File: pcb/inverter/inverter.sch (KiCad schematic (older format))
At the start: 44 parts, among them J1 Conn_01x01_Female, J2 Conn_01x01_Female, J3 Conn_01x01_Female, J4 Conn_01x01_Female, J5 Conn_01x02_Male, J6 Conn_01x02_Male, J7 Conn_01x02_Male, J8 Conn_01x02_Male, Q1 IRG4PF50W, Q2 IRG4PF50W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

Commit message: inverter PCB layout finished
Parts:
- added J1001, J1002, J1003, J1004: mounting-hole-nc, wbraun_smd:M3-through-hole, symbol wbraun_ic_lib:mounting-hole-nc
- added J1005, J1006, J1007, J1008: mounting-hole-grounded, wbraun_smd:M3-tight-fit-pan-head, symbol wbraun_ic_lib:mounting-hole-grounded
- R1, R10, R11, R12, R13, R14, R15, R16, R2, R3, R4, R5, R6, R7, R8, R9: footprint Resistor_SMD:R_0805_2012Metric -> Resistor_SMD:R_1206_3216Metric
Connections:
- net VIN+: now also J1007.1
- net VIN-: now also J1008.1
- net VSW+: now also J1005.1
- net VSW-: now also J1006.1
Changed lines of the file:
@@
 F 0 "R3" V 2900 3700 50  0000 C CNN
 F 1 "R" V 2700 3700 50  0000 C CNN
-F 2 "Resistor_SMD:R_0805_2012Metric" V 2730 3500 50  0001 C CNN
+F 2 "Resistor_SMD:R_1206_3216Metric" V 2730 3500 50  0001 C CNN
 F 3 "~" H 2800 3500 50  0001 C CNN
 	1    2800 3500
@@
 F 0 "R1" V 2850 2850 50  0000 C CNN
 F 1 "R" V 2700 2900 50  0000 C CNN
-F 2 "Resistor_SMD:R_0805_2012Metric" V 2730 2650 50  0001 C CNN
+F 2 "Resistor_SMD:R_1206_3216Metric" V 2730 2650 50  0001 C CNN
 F 3 "~" H 2800 2650 50  0001 C CNN
 	1    2800 2650
@@
 F 0 "R2" V 2593 3000 50  0000 C CNN
 F 1 "R" V 2684 3000 50  0000 C CNN
-F 2 "Resistor_SMD:R_0805_2012Metric" V 2730 3000 50  0001 C CNN
+F 2 "Resistor_SMD:R_1206_3216Metric" V 2730 3000 50  0001 C CNN
 F 3 "~" H 2800 3000 50  0001 C CNN
 	1    2800 3000
@@
 F 0 "R4" V 2593 3850 50  0000 C CNN
 F 1 "R" V 2684 3850 50  0000 C CNN
-F 2 "Resistor_SMD:R_0805_2012Metric" V 2730 3850 50  0001 C CNN
+F 2 "Resistor_SMD:R_1206_3216Metric" V 2730 3850 50  0001 C CNN
 F 3 "~" H 2800 3850 50  0001 C CNN
 	1    2800 3850
@@
 F 0 "R5" V 4250 2900 50  0000 C CNN
 F 1 "R" V 4400 2800 50  0000 C CNN
-F 2 "Resistor_SMD:R_0805_2012Metric" V 4280 2650 50  0001 C CNN
+F 2 "Resistor_SMD:R_1206_3216Metric" V 4280 2650 50  0001 C CNN
 F 3 "~" H 4350 2650 50  0001 C CNN
 	1    4350 2650
@@
 F 0 "R7" V 4150 3750 50  0000 C CNN
 F 1 "R" V 4250 3700 50  0000 C CNN
-F 2 "Resistor_SMD:R_0805_2012Metric" V 4280 3500 50  0001 C CNN
+F 2 "Resistor_SMD:R_1206_3216Metric" V 4280 3500 50  0001 C CNN
 F 3 "~" H 4350 3500 50  0001 C CNN
 	1    4350 3500
@@
 F 0 "R8" V 4143 3850 50  0000 C CNN
 F 1 "R" V 4234 3850 50  0000 C CNN
-F 2 "Resistor_SMD:R_0805_2012Metric" V 4280 3850 50  0001 C CNN
+F 2 "Resistor_SMD:R_1206_3216Metric" V 4280 3850 50  0001 C CNN
 F 3 "~" H 4350 3850 50  0001 C CNN
 	1    4350 3850
@@
 F 0 "R6" V 4143 3000 50  0000 C CNN
 F 1 "R" V 4234 3000 50  0000 C CNN
-F 2 "Resistor_SMD:R_0805_2012Metric" V 4280 3000 50  0001 C CNN
+F 2 "Resistor_SMD:R_1206_3216Metric" V 4280 3000 50  0001 C CNN
 F 3 "~" H 4350 3000 50  0001 C CNN
 	1    4350 3000
@@
 F 0 "R11" V 6700 3850 50  0000 C CNN
 F 1 "R" V 6900 3750 50  0000 C CNN
-F 2 "Resistor_SMD:R_0805_2012Metric" V 6780 3550 50  0001 C CNN
+F 2 "Resistor_SMD:R_1206_3216Metric" V 6780 3550 50  0001 C CNN
 F 3 "~" H 6850 3550 50  0001 C CNN
 	1    6850 3550
@@
 F 0 "R9" V 7000 2900 50  0000 C CNN
 F 1 "R" V 6900 2900 50  0000 C CNN
-F 2 "Resistor_SMD:R_0805_2012Metric" V 6780 2700 50  0001 C CNN
+F 2 "Resistor_SMD:R_1206_3216Metric" V 6780 2700 50  0001 C CNN
 F 3 "~" H 6850 2700 50  0001 C CNN
 	1    6850 2700
@@
 F 0 "R10" V 6643 3050 50  0000 C CNN
 F 1 "R" V 6734 3050 50  0000 C CNN
-F 2 "Resistor_SMD:R_0805_2012Metric" V 6780 3050 50  0001 C CNN
+F 2 "Resistor_SMD:R_1206_3216Metric" V 6780 3050 50  0001 C CNN
 F 3 "~" H 6850 3050 50  0001 C CNN
 	1    6850 3050
@@
 F 0 "R12" V 6643 3900 50  0000 C CNN
 F 1 "R" V 6734 3900 50  0000 C CNN
-F 2 "Resistor_SMD:R_0805_2012Metric" V 6780 3900 50  0001 C CNN
+F 2 "Resistor_SMD:R_1206_3216Metric" V 6780 3900 50  0001 C CNN
 F 3 "~" H 6850 3900 50  0001 C CNN
 	1    6850 3900
@@
 F 0 "R13" V 8200 2950 50  0000 C CNN
 F 1 "R" V 8300 2900 50  0000 C CNN
-F 2 "Resistor_SMD:R_0805_2012Metric" V 8330 2700 50  0001 C CNN
+F 2 "Resistor_SMD:R_1206_3216Metric" V 8330 2700 50  0001 C CNN
 F 3 "~" H 8400 2700 50  0001 C CNN
 	1    8400 2700
@@
 F 0 "R15" V 8300 3800 50  0000 C CNN
 F 1 "R" V 8200 3800 50  0000 C CNN
-F 2 "Resistor_SMD:R_0805_2012Metric" V 8330 3550 50  0001 C CNN
+F 2 "Resistor_SMD:R_1206_3216Metric" V 8330 3550 50  0001 C CNN
 F 3 "~" H 8400 3550 50  0001 C CNN
 	1    8400 3550
@@
 F 0 "R16" V 8193 3900 50  0000 C CNN
 F 1 "R" V 8284 3900 50  0000 C CNN
-F 2 "Resistor_SMD:R_0805_2012Metric" V 8330 3900 50  0001 C CNN
+F 2 "Resistor_SMD:R_1206_3216Metric" V 8330 3900 50  0001 C CNN
 F 3 "~" H 8400 3900 50  0001 C CNN
 	1    8400 3900
@@
 F 0 "R14" V 8193 3050 50  0000 C CNN
 F 1 "R" V 8284 3050 50  0000 C CNN
-F 2 "Resistor_SMD:R_0805_2012Metric" V 8330 3050 50  0001 C CNN
+F 2 "Resistor_SMD:R_1206_3216Metric" V 8330 3050 50  0001 C CNN
 F 3 "~" H 8400 3050 50  0001 C CNN
 	1    8400 3050
@@
 	4200 3350 4200 3500
 Connection ~ 4200 3500
+$Comp
+L wbraun_ic_lib:mounting-hole-nc J1003
+U 1 1 5C478DFD
+P 3800 4900
+F 0 "J1003" H 4078 4953 60  0000 L CNN
+F 1 "mounting-hole-nc" H 4078 4847 60  0000 L CNN
+F 2 "wbraun_smd:M3-through-hole" H 3800 4900 60  0001 C CNN
+F 3 "" H 3800 4900 60  0001 C CNN
+	1    3800 4900
+	1    0    0    -1
+$EndComp
+$Comp
+L wbraun_ic_lib:mounting-hole-nc J1001
+U 1 1 5C479324
+P 3050 4900
+F 0 "J1001" H 3328 4953 60  0000 L CNN
+F 1 "mounting-hole-nc" H 3328 4847 60  0000 L CNN
+F 2 "wbraun_smd:M3-through-hole" H 3050 4900 60  0001 C CNN
+F 3 "" H 3050 4900 60  0001 C CNN
+	1    3050 4900
+	1    0    0    -1
+$EndComp
+$Comp
+L wbraun_ic_lib:mounting-hole-nc J1002
+U 1 1 5C479727
+P 3050 5450
+F 0 "J1002" H 3328 5503 60  0000 L CNN
+F 1 "mounting-hole-nc" H 3328 5397 60  0000 L CNN
+F 2 "wbraun_smd:M3-through-hole" H 3050 5450 60  0001 C CNN
+F 3 "" H 3050 5450 60  0001 C CNN
+	1    3050 5450
+	1    0    0    -1
+$EndComp
+$Comp
+L wbraun_ic_lib:mounting-hole-nc J1004
+U 1 1 5C479B0B
+P 3800 5450
+F 0 "J1004" H 4078 5503 60  0000 L CNN
+F 1 "mounting-hole-nc" H 4078 5397 60  0000 L CNN
+F 2 "wbraun_smd:M3-through-hole" H 3800 5450 60  0001 C CNN
+F 3 "" H 3800 5450 60  0001 C CNN
+	1    3800 5450
+	1    0    0    -1
+$EndComp
+$Comp
+L wbraun_ic_lib:mounting-hole-grounded J1005
+U 1 1 5C47B16E
+P 6050 5600
+F 0 "J1005" H 6328 5547 60  0000 L CNN
+F 1 "mounting-hole-grounded" H 6328 5441 60  0000 L CNN
+F 2 "wbraun_smd:M3-tight-fit-pan-head" H 6050 5600 60  0001 C CNN
+F 3 "" H 6050 5600 60  0001 C CNN
+	1    6050 5600
+	1    0    0    -1
+$EndComp
+$Comp
+L wbraun_ic_lib:mounting-hole-grounded J1006
+U 1 1 5C47B65D
+P 7650 5600
+F 0 "J1006" H 7928 5547 60  0000 L CNN
+F 1 "mounting-hole-grounded" H 7928 5441 60  0000 L CNN
+F 2 "wbraun_smd:M3-tight-fit-pan-head" H 7650 5600 60  0001 C CNN
+F 3 "" H 7650 5600 60  0001 C CNN
+	1    7650 5600
+	1    0    0    -1
+$EndComp
+$Comp
+L wbraun_ic_lib:mounting-hole-grounded J1007
+U 1 1 5C47BD2D
+P 8700 5600
+F 0 "J1007" H 8978 5547 60  0000 L CNN
+F 1 "mounting-hole-grounded" H 8978 5441 60  0000 L CNN
+F 2 "wbraun_smd:M3-tight-fit-pan-head" H 8700 5600 60  0001 C CNN
+F 3 "" H 8700 5600 60  0001 C CNN
+	1    8700 5600
+	1    0    0    -1
+$EndComp
+$Comp
+L wbraun_ic_lib:mounting-hole-grounded J1008
+U 1 1 5C47BFA8
+P 9600 5600
+F 0 "J1008" H 9878 5547 60  0000 L CNN
+F 1 "mounting-hole-grounded" H 9878 5441 60  0000 L CNN
+F 2 "wbraun_smd:M3-tight-fit-pan-head" H 9600 5600 60  0001 C CNN
+F 3 "" H 9600 5600 60  0001 C CNN
+	1    9600 5600
+	1    0    0    -1
+$EndComp
+Wire Wire Line
+	6050 6050 6050 6150
+Wire Wire Line
+	7650 6050 7650 6150
+Wire Wire Line
+	8700 6050 8700 6150
+Wire Wire Line
+	9600 6050 9600 6150
+Text Label 6050 6150 0    50   ~ 0
+VSW+
+Text Label 7650 6150 0    50   ~ 0
+VSW-
+Text Label 8700 6150 0    50   ~ 0
+VIN+
+Text Label 9600 6150 0    50   ~ 0
+VIN-
 $EndSCHEMATC

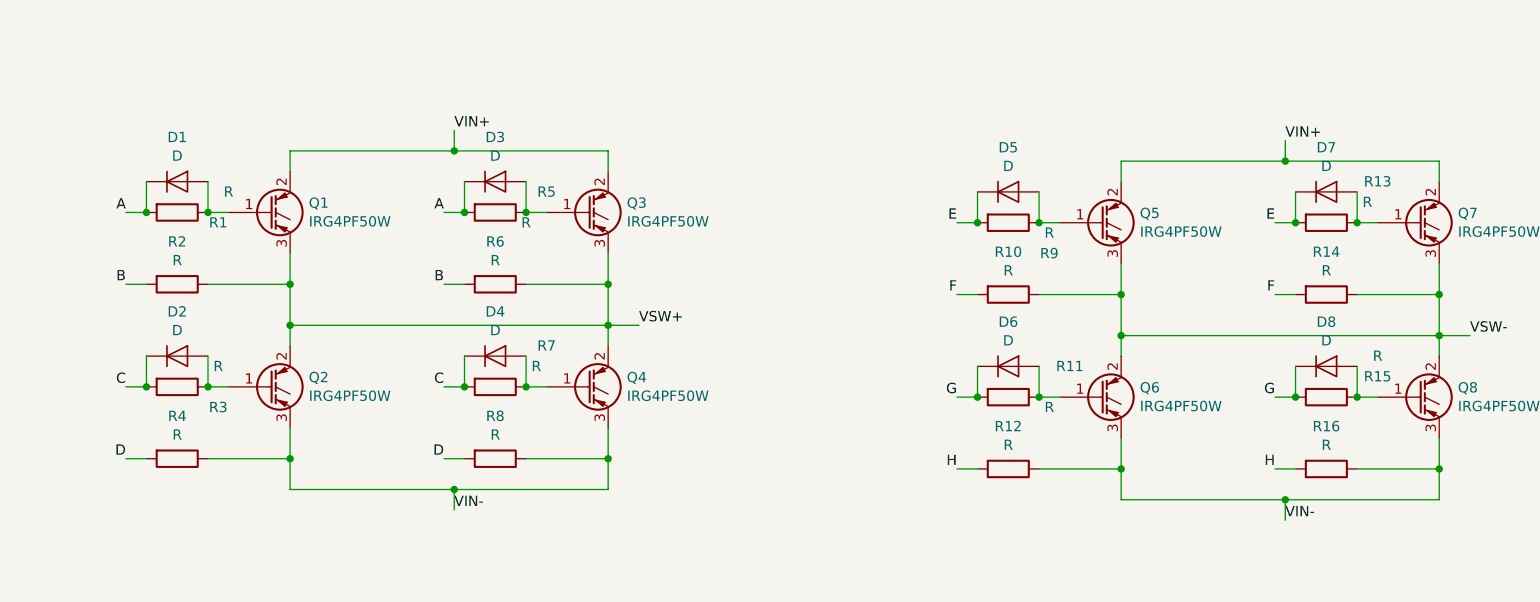
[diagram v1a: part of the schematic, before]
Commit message: updated schematic component values
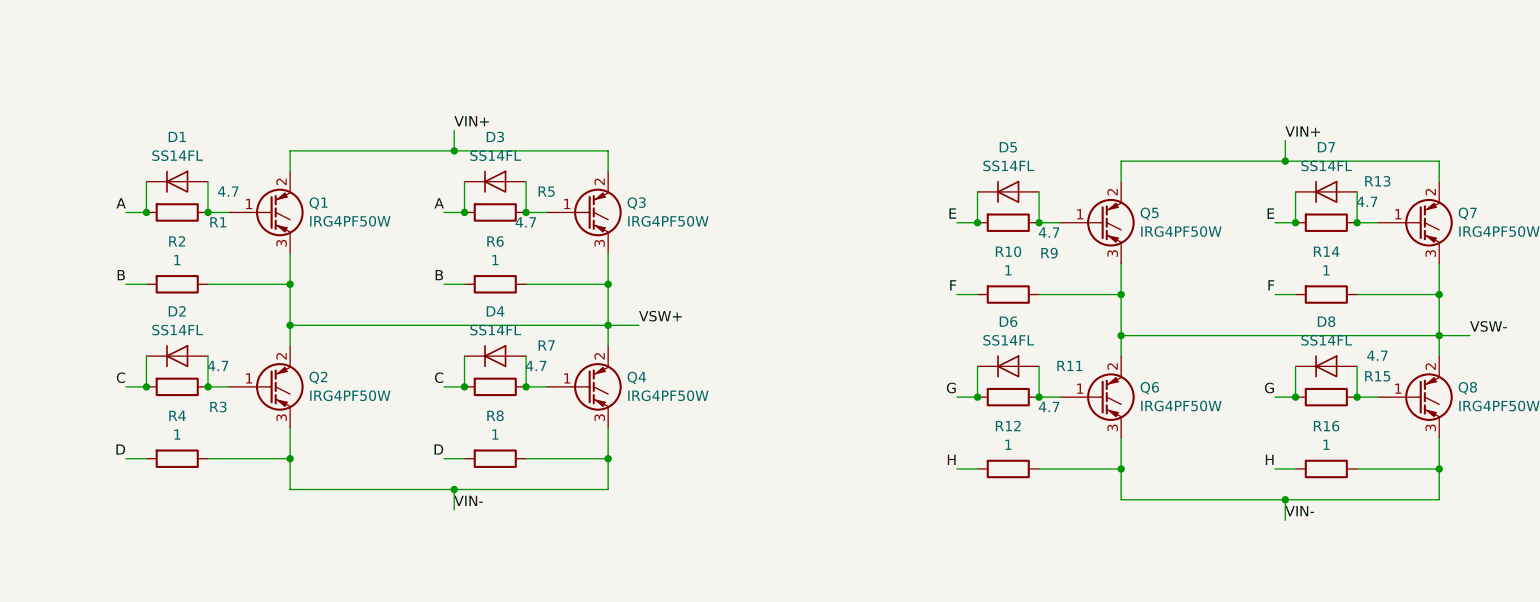
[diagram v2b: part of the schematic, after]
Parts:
- D1, D2, D3, D4, D5, D6, D7, D8: value D -> SS14FL
- R1, R11, R13, R15, R3, R5, R7, R9: value R -> 4.7
- R10, R12, R14, R16, R2, R4, R6, R8: value R -> 1
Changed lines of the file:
@@
 P 2800 3500
 F 0 "R3" V 2900 3700 50  0000 C CNN
-F 1 "R" V 2700 3700 50  0000 C CNN
+F 1 "4.7" V 2700 3700 50  0000 C CNN
 F 2 "Resistor_SMD:R_1206_3216Metric" V 2730 3500 50  0001 C CNN
 F 3 "~" H 2800 3500 50  0001 C CNN
@@
 P 2800 2650
 F 0 "R1" V 2850 2850 50  0000 C CNN
-F 1 "R" V 2700 2900 50  0000 C CNN
+F 1 "4.7" V 2700 2900 50  0000 C CNN
 F 2 "Resistor_SMD:R_1206_3216Metric" V 2730 2650 50  0001 C CNN
 F 3 "~" H 2800 2650 50  0001 C CNN
@@
 P 2800 3000
 F 0 "R2" V 2593 3000 50  0000 C CNN
-F 1 "R" V 2684 3000 50  0000 C CNN
+F 1 "1" V 2684 3000 50  0000 C CNN
 F 2 "Resistor_SMD:R_1206_3216Metric" V 2730 3000 50  0001 C CNN
 F 3 "~" H 2800 3000 50  0001 C CNN
@@
 P 2800 3850
 F 0 "R4" V 2593 3850 50  0000 C CNN
-F 1 "R" V 2684 3850 50  0000 C CNN
+F 1 "1" V 2684 3850 50  0000 C CNN
 F 2 "Resistor_SMD:R_1206_3216Metric" V 2730 3850 50  0001 C CNN
 F 3 "~" H 2800 3850 50  0001 C CNN
@@
 P 4350 2650
 F 0 "R5" V 4250 2900 50  0000 C CNN
-F 1 "R" V 4400 2800 50  0000 C CNN
+F 1 "4.7" V 4400 2800 50  0000 C CNN
 F 2 "Resistor_SMD:R_1206_3216Metric" V 4280 2650 50  0001 C CNN
 F 3 "~" H 4350 2650 50  0001 C CNN
@@
 P 4350 3500
 F 0 "R7" V 4150 3750 50  0000 C CNN
-F 1 "R" V 4250 3700 50  0000 C CNN
+F 1 "4.7" V 4250 3700 50  0000 C CNN
 F 2 "Resistor_SMD:R_1206_3216Metric" V 4280 3500 50  0001 C CNN
 F 3 "~" H 4350 3500 50  0001 C CNN
@@
 P 4350 3850
 F 0 "R8" V 4143 3850 50  0000 C CNN
-F 1 "R" V 4234 3850 50  0000 C CNN
+F 1 "1" V 4234 3850 50  0000 C CNN
 F 2 "Resistor_SMD:R_1206_3216Metric" V 4280 3850 50  0001 C CNN
 F 3 "~" H 4350 3850 50  0001 C CNN
@@
 P 4350 3000
 F 0 "R6" V 4143 3000 50  0000 C CNN
-F 1 "R" V 4234 3000 50  0000 C CNN
+F 1 "1" V 4234 3000 50  0000 C CNN
 F 2 "Resistor_SMD:R_1206_3216Metric" V 4280 3000 50  0001 C CNN
 F 3 "~" H 4350 3000 50  0001 C CNN
@@
 P 6850 3550
 F 0 "R11" V 6700 3850 50  0000 C CNN
-F 1 "R" V 6900 3750 50  0000 C CNN
+F 1 "4.7" V 6900 3750 50  0000 C CNN
 F 2 "Resistor_SMD:R_1206_3216Metric" V 6780 3550 50  0001 C CNN
 F 3 "~" H 6850 3550 50  0001 C CNN
@@
 P 6850 2700
 F 0 "R9" V 7000 2900 50  0000 C CNN
-F 1 "R" V 6900 2900 50  0000 C CNN
+F 1 "4.7" V 6900 2900 50  0000 C CNN
 F 2 "Resistor_SMD:R_1206_3216Metric" V 6780 2700 50  0001 C CNN
 F 3 "~" H 6850 2700 50  0001 C CNN
@@
 P 6850 3050
 F 0 "R10" V 6643 3050 50  0000 C CNN
-F 1 "R" V 6734 3050 50  0000 C CNN
+F 1 "1" V 6734 3050 50  0000 C CNN
 F 2 "Resistor_SMD:R_1206_3216Metric" V 6780 3050 50  0001 C CNN
 F 3 "~" H 6850 3050 50  0001 C CNN
@@
 P 6850 3900
 F 0 "R12" V 6643 3900 50  0000 C CNN
-F 1 "R" V 6734 3900 50  0000 C CNN
+F 1 "1" V 6734 3900 50  0000 C CNN
 F 2 "Resistor_SMD:R_1206_3216Metric" V 6780 3900 50  0001 C CNN
 F 3 "~" H 6850 3900 50  0001 C CNN
@@
 P 8400 2700
 F 0 "R13" V 8200 2950 50  0000 C CNN
-F 1 "R" V 8300 2900 50  0000 C CNN
+F 1 "4.7" V 8300 2900 50  0000 C CNN
 F 2 "Resistor_SMD:R_1206_3216Metric" V 8330 2700 50  0001 C CNN
 F 3 "~" H 8400 2700 50  0001 C CNN
@@
 P 8400 3550
 F 0 "R15" V 8300 3800 50  0000 C CNN
-F 1 "R" V 8200 3800 50  0000 C CNN
+F 1 "4.7" V 8200 3800 50  0000 C CNN
 F 2 "Resistor_SMD:R_1206_3216Metric" V 8330 3550 50  0001 C CNN
 F 3 "~" H 8400 3550 50  0001 C CNN
@@
 P 8400 3900
 F 0 "R16" V 8193 3900 50  0000 C CNN
-F 1 "R" V 8284 3900 50  0000 C CNN
+F 1 "1" V 8284 3900 50  0000 C CNN
 F 2 "Resistor_SMD:R_1206_3216Metric" V 8330 3900 50  0001 C CNN
 F 3 "~" H 8400 3900 50  0001 C CNN
@@
 P 8400 3050
 F 0 "R14" V 8193 3050 50  0000 C CNN
-F 1 "R" V 8284 3050 50  0000 C CNN
+F 1 "1" V 8284 3050 50  0000 C CNN
 F 2 "Resistor_SMD:R_1206_3216Metric" V 8330 3050 50  0001 C CNN
 F 3 "~" H 8400 3050 50  0001 C CNN
@@
 P 2800 2500
 F 0 "D1" H 2800 2716 50  0000 C CNN
-F 1 "D" H 2800 2625 50  0000 C CNN
+F 1 "SS14FL" H 2800 2625 50  0000 C CNN
 F 2 "Diode_SMD:D_SOD-123F" H 2800 2500 50  0001 C CNN
 F 3 "~" H 2800 2500 50  0001 C CNN
@@
 P 2800 3350
 F 0 "D2" H 2800 3566 50  0000 C CNN
-F 1 "D" H 2800 3475 50  0000 C CNN
+F 1 "SS14FL" H 2800 3475 50  0000 C CNN
 F 2 "Diode_SMD:D_SOD-123F" H 2800 3350 50  0001 C CNN
 F 3 "~" H 2800 3350 50  0001 C CNN
@@
 P 4350 3350
 F 0 "D4" H 4350 3566 50  0000 C CNN
-F 1 "D" H 4350 3475 50  0000 C CNN
+F 1 "SS14FL" H 4350 3475 50  0000 C CNN
 F 2 "Diode_SMD:D_SOD-123F" H 4350 3350 50  0001 C CNN
 F 3 "~" H 4350 3350 50  0001 C CNN
@@
 P 4350 2500
 F 0 "D3" H 4350 2716 50  0000 C CNN
-F 1 "D" H 4350 2625 50  0000 C CNN
+F 1 "SS14FL" H 4350 2625 50  0000 C CNN
 F 2 "Diode_SMD:D_SOD-123F" H 4350 2500 50  0001 C CNN
 F 3 "~" H 4350 2500 50  0001 C CNN
@@
 P 6850 2550
 F 0 "D5" H 6850 2766 50  0000 C CNN
-F 1 "D" H 6850 2675 50  0000 C CNN
+F 1 "SS14FL" H 6850 2675 50  0000 C CNN
 F 2 "Diode_SMD:D_SOD-123F" H 6850 2550 50  0001 C CNN
 F 3 "~" H 6850 2550 50  0001 C CNN
@@
 P 6850 3400
 F 0 "D6" H 6850 3616 50  0000 C CNN
-F 1 "D" H 6850 3525 50  0000 C CNN
+F 1 "SS14FL" H 6850 3525 50  0000 C CNN
 F 2 "Diode_SMD:D_SOD-123F" H 6850 3400 50  0001 C CNN
 F 3 "~" H 6850 3400 50  0001 C CNN
@@
 P 8400 3400
 F 0 "D8" H 8400 3616 50  0000 C CNN
-F 1 "D" H 8400 3525 50  0000 C CNN
+F 1 "SS14FL" H 8400 3525 50  0000 C CNN
 F 2 "Diode_SMD:D_SOD-123F" H 8400 3400 50  0001 C CNN
 F 3 "~" H 8400 3400 50  0001 C CNN
@@
 P 8400 2550
 F 0 "D7" H 8400 2766 50  0000 C CNN
-F 1 "D" H 8400 2675 50  0000 C CNN
+F 1 "SS14FL" H 8400 2675 50  0000 C CNN
 F 2 "Diode_SMD:D_SOD-123F" H 8400 2550 50  0001 C CNN
 F 3 "~" H 8400 2550 50  0001 C CNN
